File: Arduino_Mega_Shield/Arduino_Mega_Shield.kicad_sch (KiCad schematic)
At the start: 46 parts, among them J1 Conn_01x04, J10 SW10, J11 SW6, J12 SW7, J13 SW8, J14 SW9, J15 Motor Driver Connector, J16 Motor Driver Connector, J17 Motor Driver Connector, J18 Motor Driver Connector, J19 Screw_Terminal_01x02, J2 Conn_01x04, J20 JOYSTICK, J21 I2C CONNECTOR, J22 ENCODER1, J23 ENCODER2, J24 ENCODER3, J25 ENCODER4, J26 UART CONNECTOR, J3 Conn_01x04, J4 Conn_01x04, J5 SW5, J6 SW1, J7 SW2, J8 SW3, J9 SW4

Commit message: Avancement on the electric shemas and some fixe on the PCB
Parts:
- added J27, J28, J29, J30, J31, J32, J33, J34, J35, J36, J37, J38: 3_pin_selector, Arduino MCU:3 pin selector, symbol Motor_controller:3_pin_selector
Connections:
- net +12V: now also A1.8 (VMOT), A2.8 (VMOT), A3.8 (VMOT), A4.8 (VMOT)
- net +5V: now also A1.2 (VDD), A2.2 (VDD), A3.2 (VDD), A4.2 (VDD), J27.1 (Pin_1), J28.1 (Pin_1), J29.1 (Pin_1), J30.1 (Pin_1), J31.1 (Pin_1), J32.1 (Pin_1), J33.1 (Pin_1), J34.1 (Pin_1), J35.1 (Pin_1), J36.1 (Pin_1), J37.1 (Pin_1), J38.1 (Pin_1)
- net ENC_A1: now also A5.D2 (D2_INT0)
- net ENC_A2: now also A5.D3 (D3_INT1)
- net GND: now also A1.1 (GND), A1.7 (GND), A2.1 (GND), A2.7 (GND), A3.1 (GND), A3.7 (GND), A4.1 (GND), A4.7 (GND), J27.3 (Pin_3), J28.3 (Pin_3), J29.3 (Pin_3), J30.3 (Pin_3), J31.3 (Pin_3), J32.3 (Pin_3), J33.3 (Pin_3), J34.3 (Pin_3), J35.3 (Pin_3), J36.3 (Pin_3), J37.3 (Pin_3), J38.3 (Pin_3)
- net LPWM1: now also A1.16 (DIR)
- net LPWM2: now also A2.16 (DIR)
- net LPWM3: now also A3.16 (DIR)
- net LPWM4: now also A4.16 (DIR)
- net L_IS1: now also A1.14 (~{SLEEP})
- net L_IS2: now also A2.14 (~{SLEEP})
- net L_IS3: now also A3.14 (~{SLEEP})
- net L_IS4: now also A4.14 (~{SLEEP})
- net RPWM1: now also A1.15 (STEP)
- net RPWM2: now also A2.15 (STEP)
- net RPWM3: now also A3.15 (STEP)
- net RPWM4: now also A4.15 (STEP)
- net R_EN1: now also A1.9 (~{ENABLE})
- net R_EN2: now also A2.9 (~{ENABLE})
- net R_EN3: now also A3.9 (~{ENABLE})
- net R_EN4: now also A4.9 (~{ENABLE})
- net R_IS1: now also A1.13 (~{RESET})
- net R_IS2: now also A2.13 (~{RESET})
- net R_IS3: now also A3.13 (~{RESET})
- net R_IS4: now also A4.13 (~{RESET})
- net at A4.10 (MS1): now also J38.2 (Pin_2)
- net at A4.11 (MS2): now also J37.2 (Pin_2)
- net at A4.12 (MS3): now also J36.2 (Pin_2)
- net at A3.10 (MS1): now also J35.2 (Pin_2)
- net at A3.11 (MS2): now also J34.2 (Pin_2)
- net at A3.12 (MS3): now also J33.2 (Pin_2)
- net at A1.10 (MS1): now also J29.2 (Pin_2)
- net at A1.11 (MS2): now also J28.2 (Pin_2)
- net at A1.12 (MS3): now also J27.2 (Pin_2)
- net at A2.10 (MS1): now also J32.2 (Pin_2)
- net at A2.11 (MS2): now also J31.2 (Pin_2)
- net at A2.12 (MS3): now also J30.2 (Pin_2)
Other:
- moved on the sheet: A2, A3, A4, A5, BZ1, D1, J10, J11, J12, J13, J14, J15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

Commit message: Avancement in the PCB design
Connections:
- net ENC_A2: now also A5.D18 (D18/TX1); no longer A5.D3 (D3_INT1)
- net ENC_A3: now also A5.D50 (D50_MISO); no longer A5.D18 (D18/TX1)
- net ENC_A4: now also A5.D52 (D52_SCK); no longer A5.D19 (D19/RX1)
- net ENC_B1: now also A5.D3 (D3_INT1); no longer A5.D48
- net ENC_B2: now also A5.D19 (D19/RX1); no longer A5.D49
- net ENC_B3: now also A5.D51 (D51_MOSI); no longer A5.D50 (D50_MISO)
- net ENC_B4: now also A5.D53 (D53_CS); no longer A5.D51 (D51_MOSI)
- net LPWM4: now also A5.D45; no longer A5.D13
- net RPWM4: now also A5.D44; no longer A5.D12
- net SW1: now also A5.A8; no longer A5.D38
- net SW10: now also A5.D13; no longer A5.D47
- net SW2: now also A5.A9; no longer A5.D39
- net SW3: now also A5.A10; no longer A5.D40
- net SW4: now also A5.A11; no longer A5.D41
- net SW5: now also A5.A12; no longer A5.D42
- net SW6: now also A5.A13; no longer A5.D43
- net SW7: now also A5.A14; no longer A5.D44
- net SW8: now also A5.A15; no longer A5.D45
- net SW9: now also A5.D12; no longer A5.D46

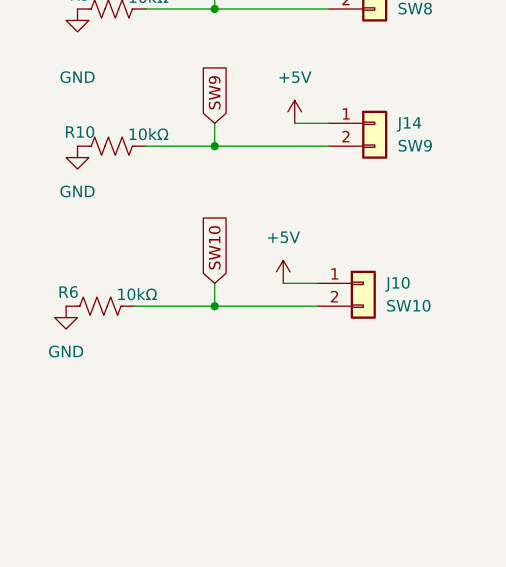
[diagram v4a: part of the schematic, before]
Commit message: Avancement on the silkscreen of the PCB
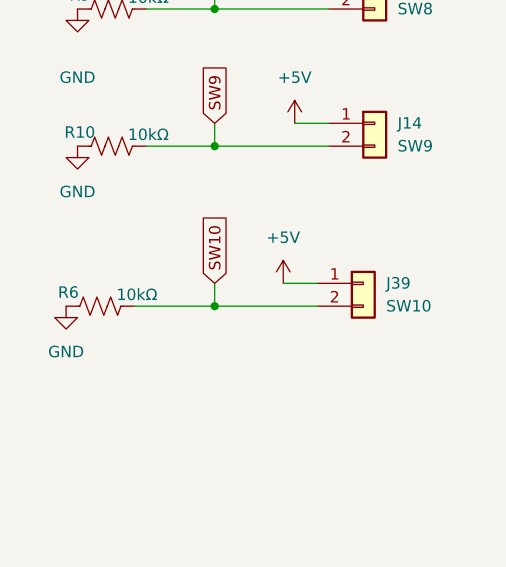
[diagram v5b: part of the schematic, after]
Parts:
- renumbered J10 to J39
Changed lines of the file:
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@@
 		(dnp no)
 		(fields_autoplaced yes)
-		(property "Reference" "J10"
+		(property "Reference" "J39"
 			(at 391.16 240.0299 0)
 			(effects
@@
 			(project "Arduino_Mega_Shield"
 				(path "/3ddd3141-4e1b-4f2a-8b19-584885bc6717"
-					(reference "J10")
+					(reference "J39")
 					(unit 1)
 				)

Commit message: improve readability of electrical shematic
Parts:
- J19: value Screw_Terminal_01x02 -> POWER INPUT
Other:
- note added: "ARDUINO MEGA"
- note added: "BUZZER AND LED"
- note added: "CONNECTORS"
- note added: "MOTORS CONTROLLERS AND ENCODERS"
- note added: "SWITCHES"
- moved on the sheet: A2, A3, A4, A5, BZ1, D1, J11, J12, J13, J14, J16, J17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
